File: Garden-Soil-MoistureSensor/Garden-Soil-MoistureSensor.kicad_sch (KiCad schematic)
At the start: 4 parts

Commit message: working on the PCB still selecting/designing things.
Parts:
- removed J?: Conn_01x02, symbol Connector_Generic:Conn_01x02
- removed R?: R, symbol Device:R
- added J3, J4: Screw_Terminal_01x02, TerminalBlock_Phoenix:TerminalBlock_Phoenix_MKDS-1,5-2_1x02_P5.00mm_Horizontal, symbol Connector:Screw_Terminal_01x02
- added Q1: BD140, Package_TO_SOT_THT:TO-126-3_Vertical, symbol Transistor_BJT:BD140
- added R1: 4.7K, Resistor_THT:R_Axial_DIN0207_L6.3mm_D2.5mm_P2.54mm_Vertical, symbol Device:R
- J1, J2: renamed from J?; footprint (none) -> Connector_PinHeader_2.54mm:PinHeader_1x15_P2.54mm_Vertical
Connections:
- net DO: now reaches J2.1 (Pin_1)
- net DO: now also J1.13 (Pin_13)
- net D7: now reaches J2.10 (Pin_10)
- net D8: now reaches J2.11 (Pin_11)
- net RX: now reaches J2.12 (Pin_12)
- net TX: now reaches J2.13 (Pin_13)
- net GND: now reaches J2.14 (Pin_14)
- net GND: now also J1.10 (Pin_10), J1.14 (Pin_14), J2.7 (Pin_7), J4.2 (Pin_2), R1.2
- net 3V#2: now reaches J2.15 (Pin_15)
- net D1: now reaches J2.2 (Pin_2)
- net D2: now reaches J2.3 (Pin_3)
- net D3: now reaches J2.4 (Pin_4)
- net D3: now also J3.1 (Pin_1)
- net D4: now reaches J2.5 (Pin_5)
- net 3V#1: now reaches J2.6 (Pin_6)
- net D5: now reaches J2.8 (Pin_8)
- net D6: now reaches J2.9 (Pin_9)
- net A0: now reaches J1.1 (Pin_1)
- net A0: now also J3.2 (Pin_2)
- net 3V#3: now reaches J1.11 (Pin_11)
- net EN: now reaches J1.12 (Pin_12)
- net VIN: now reaches J1.15 (Pin_15)
- net VIN: now also Q1.2 (C)
- net RSV1: now reaches J1.2 (Pin_2)
- net RSV2: now reaches J1.3 (Pin_3)
- net SD3: now reaches J1.4 (Pin_4)
- net SD2: now reaches J1.5 (Pin_5)
- net SD1: now reaches J1.6 (Pin_6)
- net CMD: now reaches J1.7 (Pin_7)
- net SDO: now reaches J1.8 (Pin_8)
- net CLK: now reaches J1.9 (Pin_9)
- new net: J4.1 (Pin_1), Q1.1 (E)
- new net: Q1.3 (B), R1.1
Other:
- note added: "Power Source and Reverse Polarity Protection"

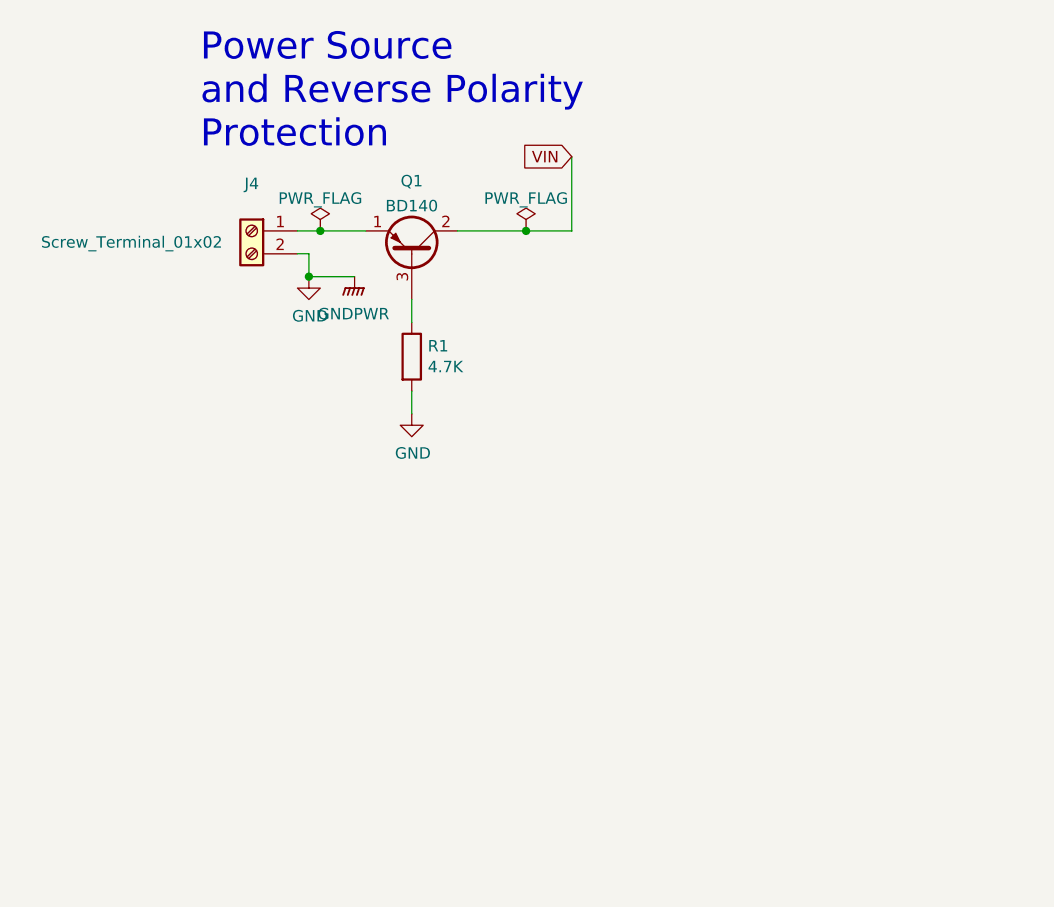
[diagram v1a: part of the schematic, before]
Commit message: adding a PCB mount 18650 battery holder.
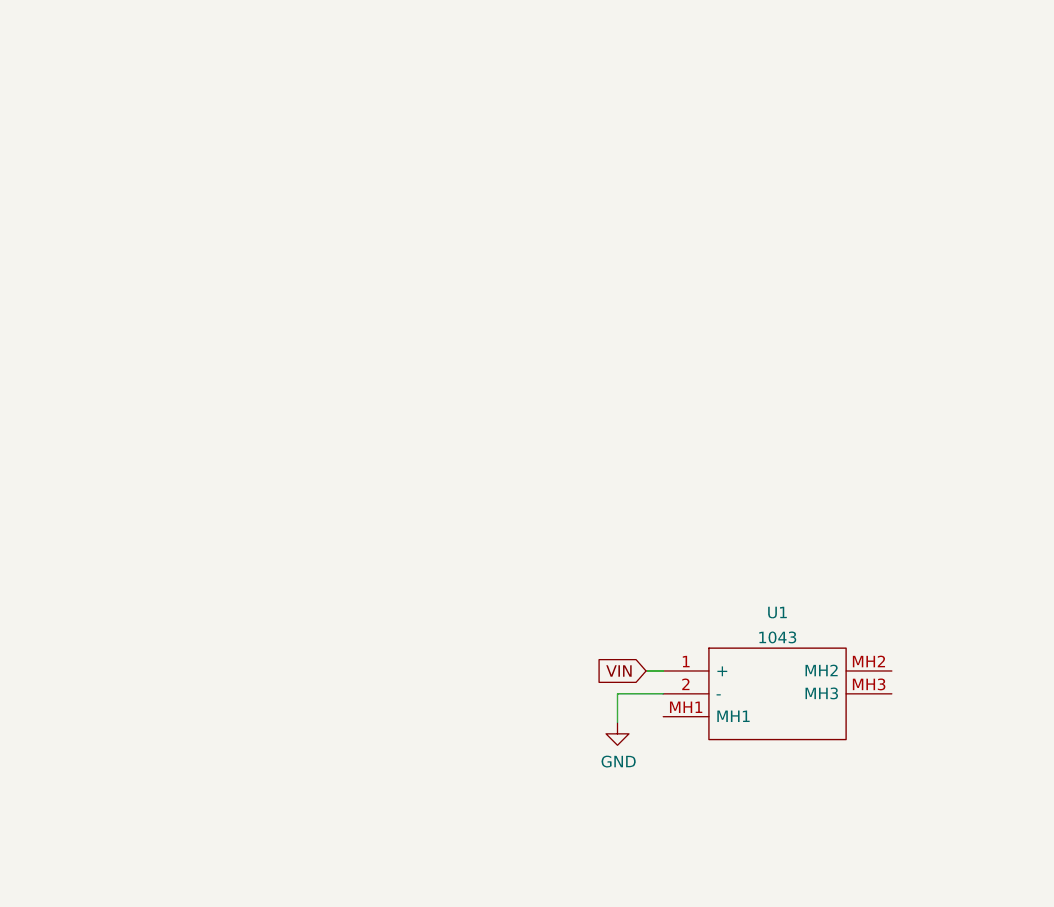
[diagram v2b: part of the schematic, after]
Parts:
- removed J4: Screw_Terminal_01x02, TerminalBlock_Phoenix:TerminalBlock_Phoenix_MKDS-1,5-2_1x02_P5.00mm_Horizontal, symbol Connector:Screw_Terminal_01x02
- removed Q1: BD140, Package_TO_SOT_THT:TO-126-3_Vertical, symbol Transistor_BJT:BD140
- removed R1: 4.7K, Resistor_THT:R_Axial_DIN0207_L6.3mm_D2.5mm_P2.54mm_Vertical, symbol Device:R
- added U1: 1043, 1043, symbol Samac_Sys:1043
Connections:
- net GND: now also U1.2 (-)
- net VIN: now also U1.1 (+)
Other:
- note removed: "Power Source and Reverse Polarity Protection"

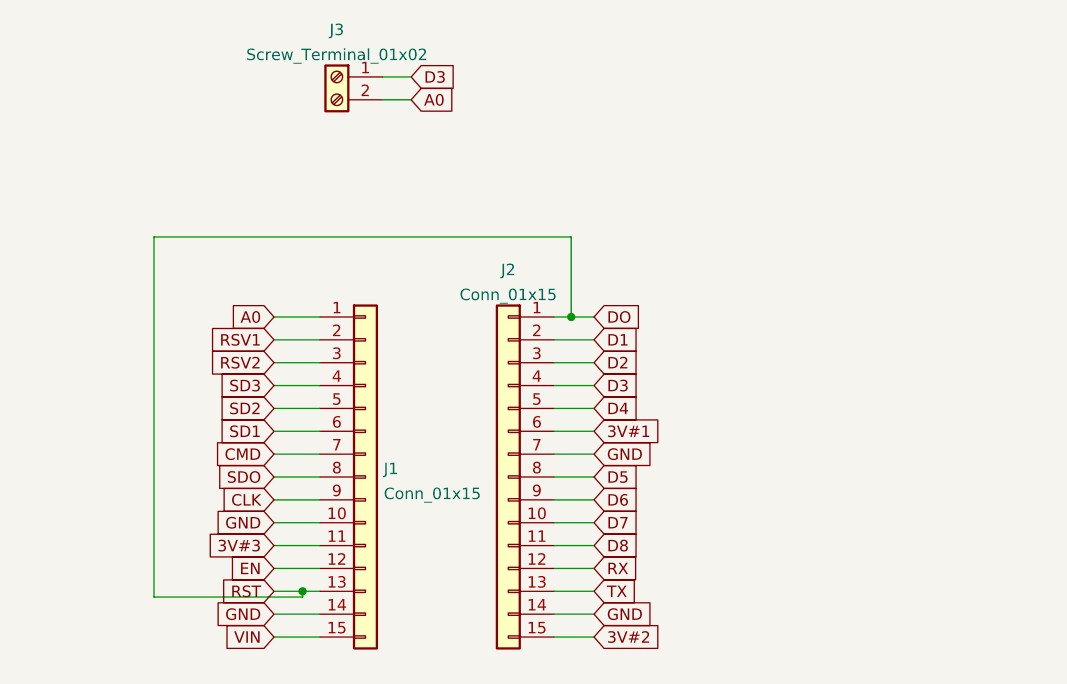
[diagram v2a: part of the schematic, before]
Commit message: adding a PCBmount 18650 battery holder. still a wip
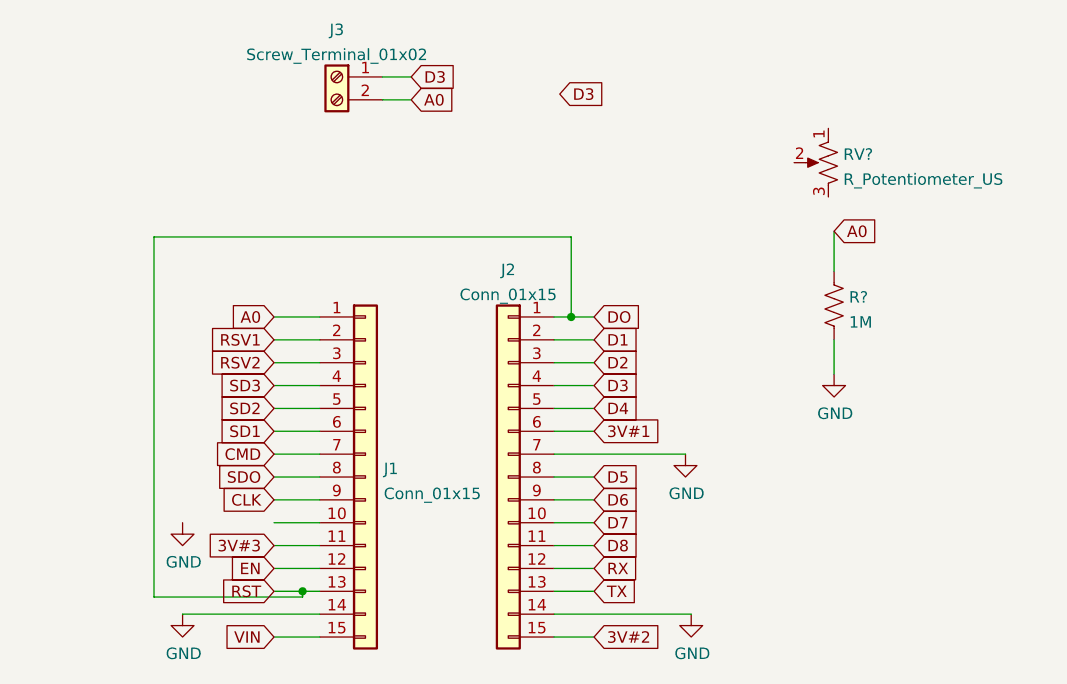
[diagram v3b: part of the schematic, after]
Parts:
- added R?: 1M, symbol Device:R_US
- added RV?: R_Potentiometer_US, symbol Device:R_Potentiometer_US
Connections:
- net A0: now also R?.1
- net GND: now also R?.2; no longer J1.10 (Pin_10)
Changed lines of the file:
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@@
+    (stroke (width 0) (type default) (color 0 0 0 0))
+  )
+  (wire (pts (xy 237.49 67.945) (xy 237.49 72.39))
     (stroke (width 0) (type default) (color 0 0 0 0))
   )
@@
     (stroke (width 0) (type default) (color 0 0 0 0))
   )
-  (wire (pts (xy 206.375 92.71) (xy 210.82 92.71))
+  (wire (pts (xy 206.375 92.71) (xy 220.98 92.71))
     (stroke (width 0) (type default) (color 0 0 0 0))
   )
@@
     (stroke (width 0) (type default) (color 0 0 0 0))
   )
-  (wire (pts (xy 175.26 110.49) (xy 180.34 110.49))
+  (wire (pts (xy 165.1 110.49) (xy 180.34 110.49))
     (stroke (width 0) (type default) (color 0 0 0 0))
   )
@@
     (stroke (width 0) (type default) (color 0 0 0 0))
   )
+  (wire (pts (xy 237.49 80.01) (xy 237.49 83.82))
+    (stroke (width 0) (type default) (color 0 0 0 0))
+  )
   (wire (pts (xy 175.26 95.25) (xy 180.34 95.25))
     (stroke (width 0) (type default) (color 0 0 0 0))
@@
     (stroke (width 0) (type default) (color 0 0 0 0))
   )
-  (wire (pts (xy 206.375 110.49) (xy 210.82 110.49))
+  (wire (pts (xy 206.375 110.49) (xy 221.615 110.49))
     (stroke (width 0) (type default) (color 0 0 0 0))
   )
@@
     (stroke (width 0) (type default) (color 0 0 0 0))
   )
-  (global_label "GND" (shape input) (at 210.82 110.49 0) (fields_autoplaced)
-    (effects (font (size 1.27 1.27)) (justify left))
-    (property "Intersheet References" "${INTERSHEET_REFS}" (id 0) (at 217.1036 110.4106 0)
-      (effects (font (size 1.27 1.27)) (justify left) hide)
-    )
-  )
   (global_label "SD3" (shape input) (at 175.26 85.09 180) (fields_autoplaced)
     (effects (font (size 1.27 1.27)) (justify right))
@@
     )
   )
+  (global_label "D3" (shape input) (at 207.01 52.705 0) (fields_autoplaced)
+    (effects (font (size 1.27 1.27)) (justify left))
+    (property "Intersheet References" "${INTERSHEET_REFS}" (id 0) (at 211.9026 52.6256 0)
+      (effects (font (size 1.27 1.27)) (justify left) hide)
+    )
+  )
   (global_label "TX" (shape input) (at 210.82 107.95 0) (fields_autoplaced)
     (effects (font (size 1.27 1.27)) (justify left))
@@
     )
   )
-  (global_label "GND" (shape input) (at 175.26 110.49 180) (fields_autoplaced)
-    (effects (font (size 1.27 1.27)) (justify right))
-    (property "Intersheet References" "${INTERSHEET_REFS}" (id 0) (at 168.9764 110.4106 0)
-      (effects (font (size 1.27 1.27)) (justify right) hide)
-    )
-  )
   (global_label "D1" (shape input) (at 210.82 80.01 0) (fields_autoplaced)
     (effects (font (size 1.27 1.27)) (justify left))
@@
     )
   )
-  (global_label "GND" (shape input) (at 210.82 92.71 0) (fields_autoplaced)
-    (effects (font (size 1.27 1.27)) (justify left))
-    (property "Intersheet References" "${INTERSHEET_REFS}" (id 0) (at 217.1036 92.6306 0)
-      (effects (font (size 1.27 1.27)) (justify left) hide)
-    )
-  )
-  (global_label "GND" (shape input) (at 175.26 100.33 180) (fields_autoplaced)
-    (effects (font (size 1.27 1.27)) (justify right))
-    (property "Intersheet References" "${INTERSHEET_REFS}" (id 0) (at 168.9764 100.2506 0)
-      (effects (font (size 1.27 1.27)) (justify right) hide)
-    )
-  )
   (global_label "VIN" (shape input) (at 92.71 90.17 180) (fields_autoplaced)
     (effects (font (size 1.27 1.27)) (justify right))
@@
     )
   )
+  (global_label "A0" (shape input) (at 237.49 67.945 0) (fields_autoplaced)
+    (effects (font (size 1.27 1.27)) (justify left))
+    (property "Intersheet References" "${INTERSHEET_REFS}" (id 0) (at 242.2012 67.8656 0)
+      (effects (font (size 1.27 1.27)) (justify left) hide)
+    )
+  )
   (global_label "A0" (shape input) (at 190.5 53.34 0) (fields_autoplaced)
     (effects (font (size 1.27 1.27)) (justify left))
@@
       (effects (font (size 1.27 1.27)) (justify right) hide)
     )
+  )
+  (symbol (lib_id "power:GND") (at 237.49 83.82 0) (unit 1)
+    (in_bom yes) (on_board yes)
+    (property "Reference" "#PWR?" (id 0) (at 237.49 90.17 0)
+      (effects (font (size 1.27 1.27)) hide)
+    )
+    (property "Value" "GND" (id 1) (at 237.617 88.2142 0))
+    (property "Footprint" "" (id 2) (at 237.49 83.82 0)
+      (effects (font (size 1.27 1.27)) hide)
+    )
+    (property "Datasheet" "" (id 3) (at 237.49 83.82 0)
+      (effects (font (size 1.27 1.27)) hide)
+    )
+    (pin "1")
   )
   (symbol (lib_id "Connector_Generic:Conn_01x15") (at 201.295 95.25 0) (mirror y) (unit 1)
@@
     (pin "9")
   )
+  (symbol (lib_id "power:GND") (at 165.1 110.49 0) (unit 1)
+    (in_bom yes) (on_board yes)
+    (property "Reference" "#PWR?" (id 0) (at 165.1 116.84 0)
+      (effects (font (size 1.27 1.27)) hide)
+    )
+    (property "Value" "GND" (id 1) (at 165.227 114.8842 0))
+    (property "Footprint" "" (id 2) (at 165.1 110.49 0)
+      (effects (font (size 1.27 1.27)) hide)
+    )
+    (property "Datasheet" "" (id 3) (at 165.1 110.49 0)
+      (effects (font (size 1.27 1.27)) hide)
+    )
+    (pin "1")
+  )
   (symbol (lib_id "Samac_Sys:1043") (at 94.615 90.17 0) (unit 1)
     (in_bom yes) (on_board yes) (fields_autoplaced)
@@
     (pin "MH2")
     (pin "MH3")
+  )
+  (symbol (lib_id "Device:R_Potentiometer_US") (at 236.855 60.325 0) (mirror y) (unit 1)
+    (in_bom yes) (on_board yes) (fields_autoplaced)
+    (property "Reference" "RV?" (id 0) (at 238.506 59.4165 0)
+      (effects (font (size 1.27 1.27)) (justify right))
+    )
+    (property "Value" "R_Potentiometer_US" (id 1) (at 238.506 62.1916 0)
+      (effects (font (size 1.27 1.27)) (justify right))
+    )
+    (property "Footprint" "" (id 2) (at 236.855 60.325 0)
+      (effects (font (size 1.27 1.27)) hide)
+    )
+    (property "Datasheet" "~" (id 3) (at 236.855 60.325 0)
+      (effects (font (size 1.27 1.27)) hide)
+    )
+    (pin "1")
+    (pin "2")
+    (pin "3")
+  )
+  (symbol (lib_id "power:GND") (at 221.615 110.49 0) (unit 1)
+    (in_bom yes) (on_board yes)
+    (property "Reference" "#PWR?" (id 0) (at 221.615 116.84 0)
+      (effects (font (size 1.27 1.27)) hide)
+    )
+    (property "Value" "GND" (id 1) (at 221.742 114.8842 0))
+    (property "Footprint" "" (id 2) (at 221.615 110.49 0)
+      (effects (font (size 1.27 1.27)) hide)
+    )
+    (property "Datasheet" "" (id 3) (at 221.615 110.49 0)
+      (effects (font (size 1.27 1.27)) hide)
+    )
+    (pin "1")
   )
   (symbol (lib_id "power:GND") (at 89.535 95.885 0) (unit 1)
@@
     (pin "9")
   )
+  (symbol (lib_id "power:GND") (at 165.1 100.33 0) (unit 1)
+    (in_bom yes) (on_board yes)
+    (property "Reference" "#PWR?" (id 0) (at 165.1 106.68 0)
+      (effects (font (size 1.27 1.27)) hide)
+    )
+    (property "Value" "GND" (id 1) (at 165.227 104.7242 0))
+    (property "Footprint" "" (id 2) (at 165.1 100.33 0)
+      (effects (font (size 1.27 1.27)) hide)
+    )
+    (property "Datasheet" "" (id 3) (at 165.1 100.33 0)
+      (effects (font (size 1.27 1.27)) hide)
+    )
+    (pin "1")
+  )
+  (symbol (lib_id "power:GND") (at 220.98 92.71 0) (unit 1)
+    (in_bom yes) (on_board yes)
+    (property "Reference" "#PWR?" (id 0) (at 220.98 99.06 0)
+      (effects (font (size 1.27 1.27)) hide)
+    )
+    (property "Value" "GND" (id 1) (at 221.107 97.1042 0))
+    (property "Footprint" "" (id 2) (at 220.98 92.71 0)
+      (effects (font (size 1.27 1.27)) hide)
+    )
+    (property "Datasheet" "" (id 3) (at 220.98 92.71 0)
+      (effects (font (size 1.27 1.27)) hide)
+    )
+    (pin "1")
+  )
+  (symbol (lib_id "Device:R_US") (at 237.49 76.2 0) (unit 1)
+    (in_bom yes) (on_board yes) (fields_autoplaced)
+    (property "Reference" "R?" (id 0) (at 239.141 75.2915 0)
+      (effects (font (size 1.27 1.27)) (justify left))
+    )
+    (property "Value" "1M" (id 1) (at 239.141 78.0666 0)
+      (effects (font (size 1.27 1.27)) (justify left))
+    )
+    (property "Footprint" "" (id 2) (at 238.506 76.454 90)
+      (effects (font (size 1.27 1.27)) hide)
+    )
+    (property "Datasheet" "~" (id 3) (at 237.49 76.2 0)
+      (effects (font (size 1.27 1.27)) hide)
+    )
+    (pin "1")
+    (pin "2")
+  )
   (symbol (lib_id "Connector:Screw_Terminal_01x02") (at 182.245 50.8 0) (mirror y) (unit 1)
     (in_bom yes) (on_board yes) (fields_autoplaced)
@@
       (reference "#PWR0101") (unit 1) (value "GND") (footprint "")
     )
+    (path "/0d8df86c-0791-4795-8a7f-3b35c3bd23b6"
+      (reference "#PWR?") (unit 1) (value "GND") (footprint "")
+    )
+    (path "/4d78dbb5-f813-4c91-8664-f3c18aaf25b6"
+      (reference "#PWR?") (unit 1) (value "GND") (footprint "")
+    )
+    (path "/92325887-faf4-48b7-aae7-aad9eab88395"
+      (reference "#PWR?") (unit 1) (value "GND") (footprint "")
+    )
+    (path "/cb146cd0-c332-43d8-80c7-0b53cc1210ff"
+      (reference "#PWR?") (unit 1) (value "GND") (footprint "")
+    )
+    (path "/d41ff435-54dc-4373-b17e-48692788c5db"
+      (reference "#PWR?") (unit 1) (value "GND") (footprint "")
+    )
     (path "/c24d6ac8-802d-4df3-a210-9cb1f693e865"
       (reference "J1") (unit 1) (value "Conn_01x15") (footprint "Connector_PinHeader_2.54mm:PinHeader_1x15_P2.54mm_Vertical")
@@
       (reference "J3") (unit 1) (value "Screw_Terminal_01x02") (footprint "TerminalBlock_Phoenix:TerminalBlock_Phoenix_MKDS-1,5-2_1x02_P5.00mm_Horizontal")
     )
+    (path "/d90db84e-7df3-4d1b-b263-27f7c3991121"
+      (reference "R?") (unit 1) (value "1M") (footprint "")
+    )
+    (path "/61fae217-e18a-4e68-8630-42cc06a8ba2f"
+      (reference "RV?") (unit 1) (value "R_Potentiometer_US") (footprint "")
+    )
     (path "/5b70b09b-6762-4725-9d48-805300c0bdc8"

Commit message: wip on adding the MUXes.
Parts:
- removed J3: Screw_Terminal_01x02, TerminalBlock_Phoenix:TerminalBlock_Phoenix_MKDS-1,5-2_1x02_P5.00mm_Horizontal, symbol Connector:Screw_Terminal_01x02
- removed RV?: R_Potentiometer_US, symbol Device:R_Potentiometer_US
- added IC? (x2): CD74HC4067M96, SOIC127P1030X265-24N, symbol Samac_Sys:CD74HC4067M96
- added R?: 10K, symbol Device:R_US
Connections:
- net A0: now also IC?.1 (COMMON_INPUT/OUTPUT)
- net D1: now also IC?.10 (S0), IC?.10 (S0)
- net D2: now also IC?.11 (S1), IC?.11 (S1)
- net D3: now also IC?.14 (S2), IC?.14 (S2)
- net D4: now also IC?.13 (S3), IC?.13 (S3)
- net D7: now also IC?.15 (~{E}), IC?.15 (~{E})
- net GND: now also J1.10 (Pin_10), IC?.12 (GND), IC?.12 (GND)
- net VIN: now also IC?.24 (VCC), IC?.24 (VCC), R?.1
- new net: IC?.1 (COMMON_INPUT/OUTPUT), R?.2
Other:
- moved on the sheet: R?, U1
